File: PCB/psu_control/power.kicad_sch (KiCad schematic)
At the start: 37 parts

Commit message: psu_control v4 is completed
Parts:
- removed J?: Vout (10-25V), symbol Connector:Conn_01x02_Male
- added R39: 698, Resistor_SMD:R_0805_2012Metric, symbol Device:R
- added R40, R41: 2.2k, Resistor_SMD:R_0805_2012Metric, symbol Device:R
- C1, C2, C3, C4, C7: renamed from C?; footprint (none) -> Capacitor_SMD:C_0805_2012Metric
- C5: renamed from C?; footprint (none) -> Capacitor_THT:CP_Radial_D6.3mm_P2.50mm
- C6: renamed from C?; footprint (none) -> Capacitor_THT:CP_Radial_D10.0mm_P5.00mm
- F1: renamed from F?; footprint (none) -> t-top:M205_FUSE
- J1, J2, J4: renamed from J?; footprint (none) -> t-top:OSTTA020161
- J3: renamed from J?; footprint (none) -> Connector_JST:JST_XH_B2B-XH-A_1x02_P2.50mm_Vertical
- L1: renamed from L?; footprint (none) -> t-top:NS12575T220MN
- Q2: renamed from Q?; footprint (none) -> Package_TO_SOT_SMD:TO-252-2
- Q3: renamed from Q?; footprint (none) -> Package_TO_SOT_SMD:SOT-23
- R10, R7, R8, R9: renamed from R?; value 10 -> 0; footprint (none) -> Resistor_SMD:R_0805_2012Metric
- R11, R12, R13, R15, R18, R5, R6: renamed from R?; footprint (none) -> Resistor_SMD:R_0805_2012Metric
- R14: renamed from R?; footprint (none) -> Resistor_SMD:R_1206_3216Metric
- R16, R17, R19, R20: renamed from R?; value 10 -> NI; footprint (none) -> Resistor_SMD:R_0805_2012Metric
- SW1: renamed from SW?; value Power DPST -> Non-Momentary DPST; footprint (none) -> Connector_JST:JST_PH_B4B-PH-K_1x04_P2.00mm_Vertical
- U3: renamed from U?; footprint (none) -> Package_SO:VSSOP-10_3x3mm_P0.5mm
- U4: renamed from U?; footprint (none) -> t-top:K7805-3AR3
- U5: renamed from U?; footprint (none) -> Package_SO:TSSOP-14_4.4x5mm_P0.65mm
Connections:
- net +3.3V: now also R40.1, R41.1
- net GENERAL_SCL: now also R41.2
- net GENERAL_SDA: now also R40.2
- net ~{POWER_OFF}: now also R39.1; no longer Q3.1 (G), R13.1
- net at R11.2, R14.1, U3.8 (VBUS): no longer Q2.2 (D)
- new net: Q3.1 (G), R13.1, R39.2
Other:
- note added: "1000000: R7=NI, R9=0, R8=NI, R10=0 1000001: R7=NI, R9=0, R8=0, R10=NI 1000100: R7=0, R9=NI, R8=NI, R10=0 1000101: R7=0, R9=NI, R8=0, R10=NI NI: Not Installed"
- note added: "J1: Screw Terminal SW1: JST PH Connector"
- note added: "J2 : Screw Terminal J3 : Screw Terminal J4 : Screw Terminal"
- note removed: "1000000: R?=NI, R?=0, R?=NI, R?=0 1000001: R?=NI, R?=0, R?=0, R?=NI 1000100: R?=0, R?=NI, R?=NI, R?=0 1000101: R?=0, R?=NI, R?=0, R?=NI NI: Not Installed"
- moved on the sheet: C1, C2, C3, C7, F1, J1, Q2, Q3, R10, R11, R12, R13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

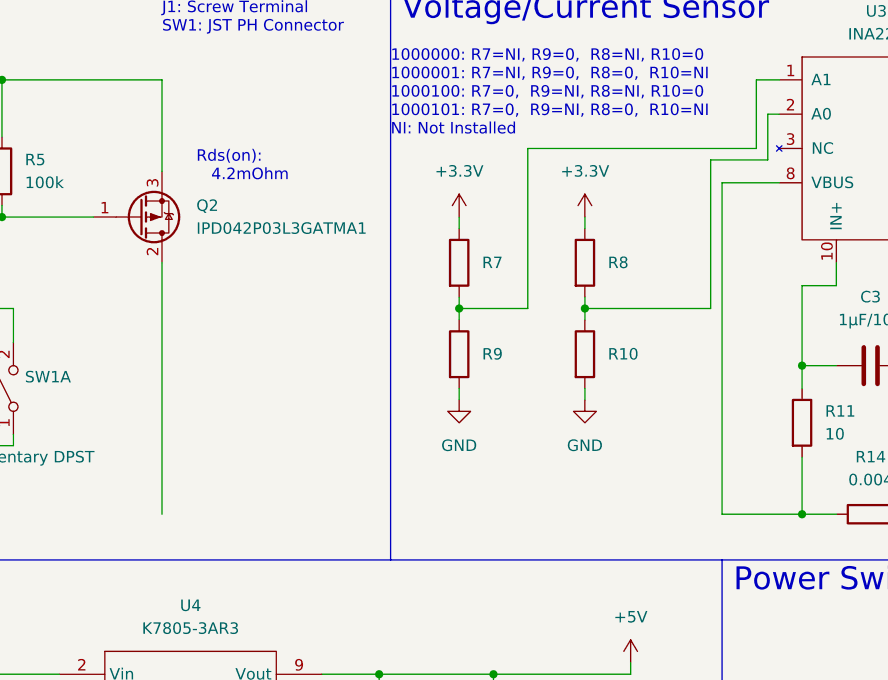
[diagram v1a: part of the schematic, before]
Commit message: Add dynamixel_control PCB
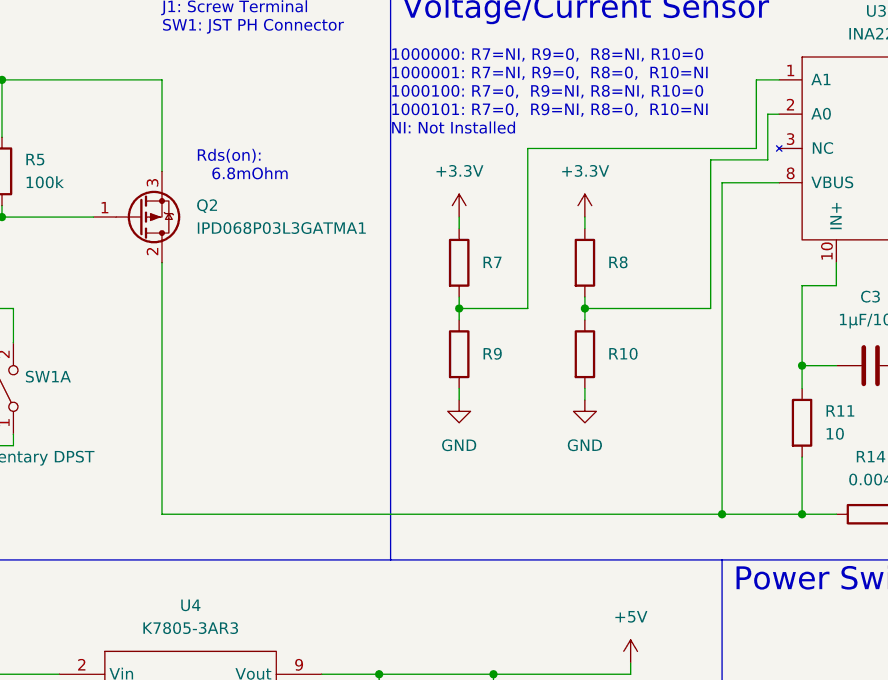
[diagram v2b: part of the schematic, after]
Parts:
- Q2: value IPD042P03L3GATMA1 -> IPD068P03L3GATMA1
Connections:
- net at Q2.2 (D): now also R11.2, R14.1, U3.8 (VBUS)
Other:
- note added: "Rds(on): 6.8mOhm"
- note removed: "Rds(on): 4.2mOhm"
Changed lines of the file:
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@@
   (junction (at 49.53 54.61) (diameter 0) (color 0 0 0 0)
   )
+  (junction (at 158.75 71.12) (diameter 0) (color 0 0 0 0)
+  )
   (junction (at 59.69 38.1) (diameter 0) (color 0 0 0 0)
   )
@@
   )
   (wire (pts (xy 203.2 30.48) (xy 204.47 30.48))
+    (stroke (width 0) (type default) (color 0 0 0 0))
+  )
+  (wire (pts (xy 96.52 71.12) (xy 158.75 71.12))
     (stroke (width 0) (type default) (color 0 0 0 0))
   )
@@
     (effects (font (size 2.54 2.54)) (justify left bottom))
   )
-  (text "Rds(on):\n   4.2mOhm" (at 100.33 34.29 0)
+  (text "Rds(on):\n   6.8mOhm" (at 100.33 34.29 0)
     (effects (font (size 1.27 1.27)) (justify left bottom))
   )
@@
       (effects (font (size 1.27 1.27)) (justify left))
     )
-    (property "Value" "IPD042P03L3GATMA1" (id 1) (at 100.33 39.3699 0)
+    (property "Value" "IPD068P03L3GATMA1" (id 1) (at 100.33 39.3699 0)
       (effects (font (size 1.27 1.27)) (justify left))
     )

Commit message: Fix issues. Add schematic files.
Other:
- note added: "I2C Address 1000000: R7=NI, R9=0, R8=NI, R10=0 1000001: R7=NI, R9=0, R8=0, R10=NI 1000100: R7=0, R9=NI, R8=NI, R10=0 1000101: R7=0, R9=NI, R8=0, R10=NI NI: Not Installed"
- note removed: "1000000: R7=NI, R9=0, R8=NI, R10=0 1000001: R7=NI, R9=0, R8=0, R10=NI 1000100: R7=0, R9=NI, R8=NI, R10=0 1000101: R7=0, R9=NI, R8=0, R10=NI NI: Not Installed"
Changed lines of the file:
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@@
     (effects (font (size 2.54 2.54)) (justify left bottom))
   )
-  (text "1000000: R7=NI, R9=0,  R8=NI, R10=0\n1000001: R7=NI, R9=0,  R8=0,  R10=NI\n1000100: R7=0,  R9=NI, R8=NI, R10=0\n1000101: R7=0,  R9=NI, R8=0,  R10=NI\nNI: Not Installed"
+  (text "I2C Address\n1000000: R7=NI, R9=0,  R8=NI, R10=0\n1000001: R7=NI, R9=0,  R8=0,  R10=NI\n1000100: R7=0,  R9=NI, R8=NI, R10=0\n1000101: R7=0,  R9=NI, R8=0,  R10=NI\nNI: Not Installed"
     (at 121.92 29.21 0)
     (effects (font (size 1.27 1.27)) (justify left bottom))

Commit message: Fix PCBs.
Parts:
- removed J3: Vout (5V), Connector_JST:JST_XH_B2B-XH-A_1x02_P2.50mm_Vertical, symbol Connector:Conn_01x02_Male
- added C23, C9: 100µF/35V, Capacitor_THT:CP_Radial_D6.3mm_P2.50mm, symbol Device:C_Polarized
- added C31: 22μF/10V, Capacitor_SMD:C_0805_2012Metric, symbol Device:C
- added L2: 22µH (NS12575T220MN), t-top:NS12575T220MN, symbol Device:L_Ferrite
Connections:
- net +5V: now also C23.1, C31.1, L2.2; no longer C4.1, R17.1, U4.9 (Vout)
- net GND: now also C23.2, C31.2, C9.2
- new net: C4.1, C9.1, L2.1, R17.1, U4.9 (Vout)
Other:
- moved on the sheet: C7, R15, R18, SW1B, U5F

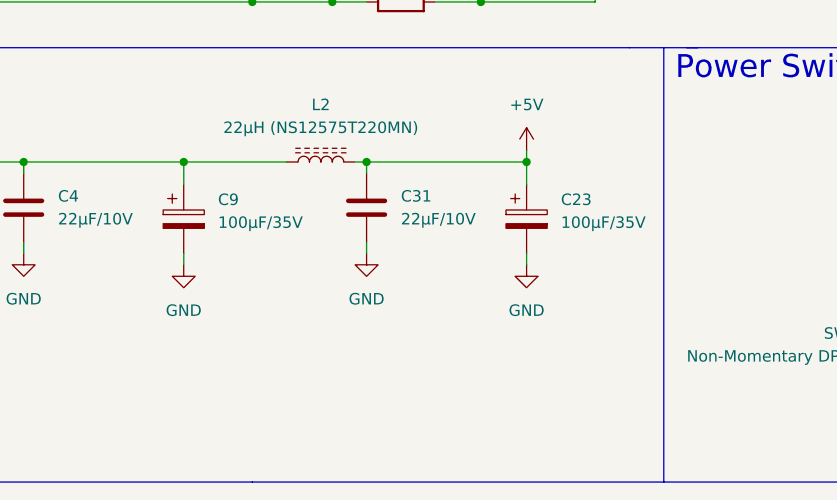
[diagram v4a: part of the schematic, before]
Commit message: Add a PI filter to buck_boost. Fix ringing for other PI filters.
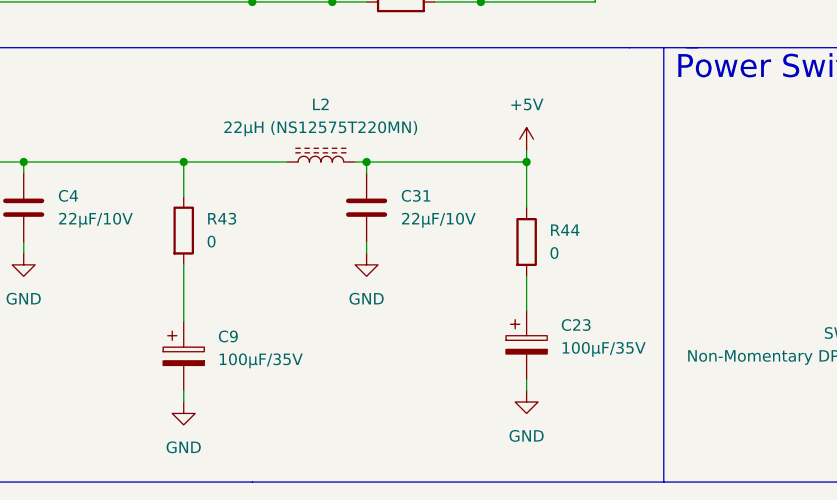
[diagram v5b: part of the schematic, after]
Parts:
- added R43, R44: 0, Resistor_SMD:R_1206_3216Metric, symbol Device:R
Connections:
- net +5V: now also R44.1; no longer C23.1
- net at C4.1, L2.1, R17.1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: now also R43.1; no longer C9.1
- new net: C9.1, R43.2
- new net: C23.1, R44.2
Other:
- moved on the sheet: C23, C9

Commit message: Update PCBs
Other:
- note added: "J2 : Screw Terminal J4 : Screw Terminal"
- note removed: "J2 : Screw Terminal J3 : Screw Terminal J4 : Screw Terminal"
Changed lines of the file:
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@@
     (effects (font (size 2.54 2.54)) (justify left bottom))
   )
-  (text "J2 : Screw Terminal\nJ3 : Screw Terminal\nJ4 : Screw Terminal\n"
-    (at 264.16 74.93 0)
+  (text "J2 : Screw Terminal\nJ4 : Screw Terminal\n" (at 264.16 74.93 0)
     (effects (font (size 1.27 1.27)) (justify left bottom))
   )

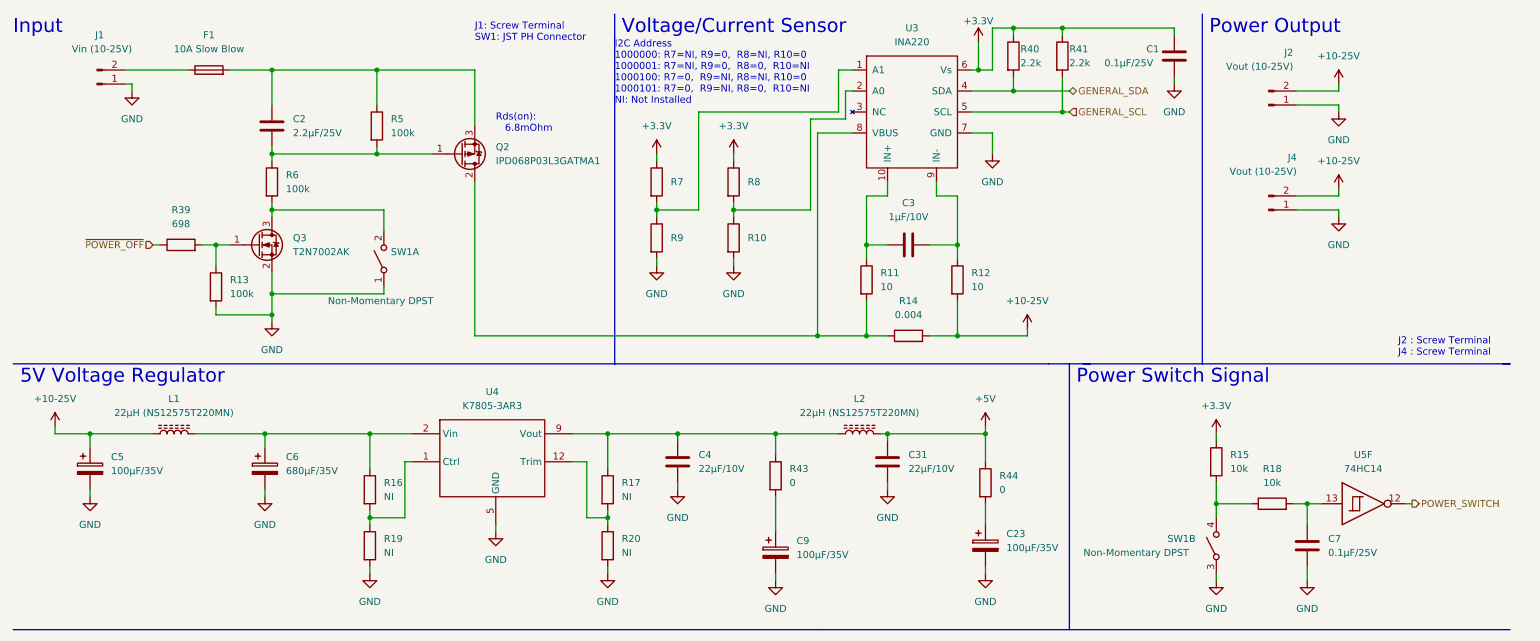
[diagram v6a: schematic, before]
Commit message: Fix the psu_control PCB.
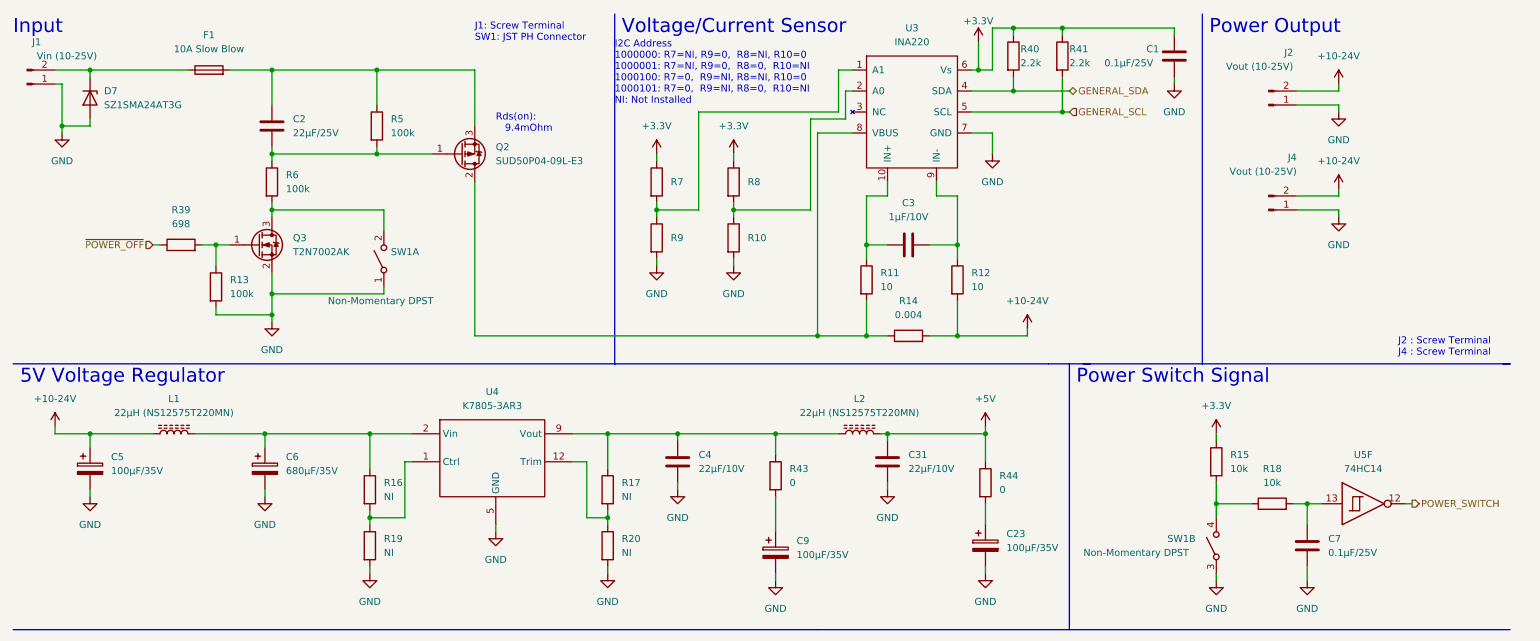
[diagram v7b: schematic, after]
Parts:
- added D7: SZ1SMA24AT3G, Diode_SMD:D_SMA, symbol Device:D_Zener
- C2: value 2.2µF/25V -> 22µF/25V
- Q2: value IPD068P03L3GATMA1 -> SUD50P04-09L-E3
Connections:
- net GND: now also D7.2 (A)
- net at F1.1, J1.2 (Pin_2): now also D7.1 (K)
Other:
- note added: "Rds(on): 9.4mOhm"
- note removed: "Rds(on): 6.8mOhm"
- moved on the sheet: J1

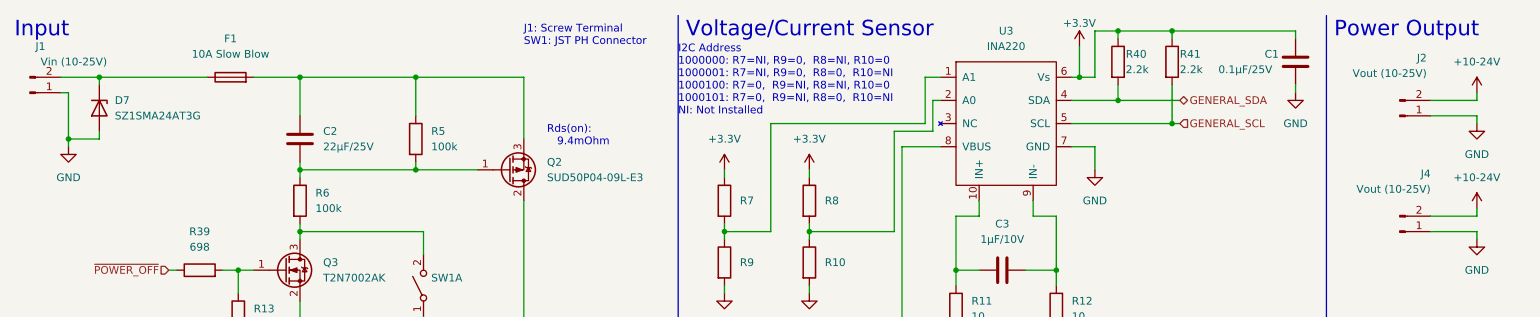
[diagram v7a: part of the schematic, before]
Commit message: Fix the max input voltage in the psu_control PCB.
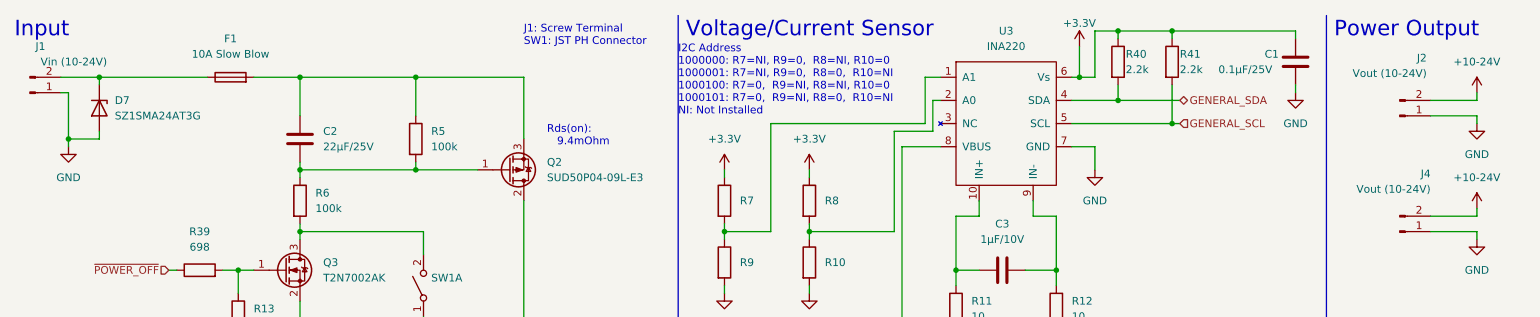
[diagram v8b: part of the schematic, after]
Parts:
- J1: value Vin (10-25V) -> Vin (10-24V)
- J2, J4: value Vout (10-25V) -> Vout (10-24V)
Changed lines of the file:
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@@
       (effects (font (size 1.27 1.27)) (justify right))
     )
-    (property "Value" "Vin (10-25V)" (id 1) (at 27.94 20.32 0)
+    (property "Value" "Vin (10-24V)" (id 1) (at 27.94 20.32 0)
       (effects (font (size 1.27 1.27)) (justify right))
     )
@@
       (effects (font (size 1.27 1.27)) (justify right))
     )
-    (property "Value" "Vout (10-25V)" (id 1) (at 245.745 41.275 0)
+    (property "Value" "Vout (10-24V)" (id 1) (at 245.745 41.275 0)
       (effects (font (size 1.27 1.27)) (justify right))
     )
@@
       (effects (font (size 1.27 1.27)) (justify right))
     )
-    (property "Value" "Vout (10-25V)" (id 1) (at 245.11 22.225 0)
-      (effects (font (size 1.27 1.27)) (justify right))
-    )
+    (property "Value" "Vout (10-24V)" (id 1) (at 245.11 22.225 0)
+      (effects (font (size 1.27 1.27)) (justify right))
+    )
